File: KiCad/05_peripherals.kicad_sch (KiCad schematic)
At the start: 35 parts, among them IC501 VEML7700-TT, IC502 DS3231MZ+TRL, U502 DS18B20, U503 LM35-LP, U504 DHT11

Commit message: Layout updates
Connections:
- net +3V3 is gone; now on net +3V3_PER: SW501.1, SW501.4, SW502.1, SW502.4, SW503.1, SW503.4
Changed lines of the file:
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@@
 	)
 	(symbol
+		(lib_id "power:+3.3V")
+		(at 55.88 167.64 0)
+		(unit 1)
+		(exclude_from_sim no)
+		(in_bom yes)
+		(on_board yes)
+		(dnp no)
+		(property "Reference" "#PWR02"
+			(at 55.88 171.45 0)
+			(effects
+				(font
+					(size 1.27 1.27)
+				)
+				(hide yes)
+			)
+		)
+		(property "Value" "+3V3_PER"
+			(at 61.214 166.878 0)
+			(effects
+				(font
+					(size 1.27 1.27)
+				)
+			)
+		)
+		(property "Footprint" ""
+			(at 55.88 167.64 0)
+			(effects
+				(font
+					(size 1.27 1.27)
+				)
+				(hide yes)
+			)
+		)
+		(property "Datasheet" ""
+			(at 55.88 167.64 0)
+			(effects
+				(font
+					(size 1.27 1.27)
+				)
+				(hide yes)
+			)
+		)
+		(property "Description" "Power symbol creates a global label with name \"+3.3V\""
+			(at 55.88 167.64 0)
+			(effects
+				(font
+					(size 1.27 1.27)
+				)
+				(hide yes)
+			)
+		)
+		(pin "1"
+		)
+		(instances
+			(project "esp32_s3_weather_webserver"
+				(path "/04e96486-ec4c-4881-a0bf-37cb6ce91c2d/c3c48617-55df-481a-bcdd-56b688125780"
+					(reference "#PWR02")
+					(unit 1)
+				)
+			)
+		)
+	)
+	(symbol
 		(lib_id "power:GND")
 		(at 205.74 116.84 0)
@@
 	)
 	(symbol
-		(lib_id "power:+3.3V")
-		(at 17.78 167.64 0)
-		(unit 1)
-		(exclude_from_sim no)
-		(in_bom yes)
-		(on_board yes)
-		(dnp no)
-		(property "Reference" "#PWR0528"
-			(at 17.78 171.45 0)
-			(effects
-				(font
-					(size 1.27 1.27)
-				)
-				(hide yes)
-			)
-		)
-		(property "Value" "+3V3"
-			(at 17.526 164.338 0)
-			(effects
-				(font
-					(size 1.27 1.27)
-				)
-			)
-		)
-		(property "Footprint" ""
-			(at 17.78 167.64 0)
-			(effects
-				(font
-					(size 1.27 1.27)
-				)
-				(hide yes)
-			)
-		)
-		(property "Datasheet" ""
-			(at 17.78 167.64 0)
-			(effects
-				(font
-					(size 1.27 1.27)
-				)
-				(hide yes)
-			)
-		)
-		(property "Description" "Power symbol creates a global label with name \"+3.3V\""
-			(at 17.78 167.64 0)
-			(effects
-				(font
-					(size 1.27 1.27)
-				)
-				(hide yes)
-			)
-		)
-		(pin "1"
-		)
-		(instances
-			(project "esp32_s3_weather_webserver"
-				(path "/04e96486-ec4c-4881-a0bf-37cb6ce91c2d/c3c48617-55df-481a-bcdd-56b688125780"
-					(reference "#PWR0528")
-					(unit 1)
-				)
-			)
-		)
-	)
-	(symbol
 		(lib_id "esp32_s3_weather_webserver:SW_PUSH_6mm_H5mm")
 		(at 25.4 175.26 0)
@@
 	)
 	(symbol
+		(lib_id "power:+3.3V")
+		(at 99.06 167.64 0)
+		(unit 1)
+		(exclude_from_sim no)
+		(in_bom yes)
+		(on_board yes)
+		(dnp no)
+		(property "Reference" "#PWR01"
+			(at 99.06 171.45 0)
+			(effects
+				(font
+					(size 1.27 1.27)
+				)
+				(hide yes)
+			)
+		)
+		(property "Value" "+3V3_PER"
+			(at 104.394 166.878 0)
+			(effects
+				(font
+					(size 1.27 1.27)
+				)
+			)
+		)
+		(property "Footprint" ""
+			(at 99.06 167.64 0)
+			(effects
+				(font
+					(size 1.27 1.27)
+				)
+				(hide yes)
+			)
+		)
+		(property "Datasheet" ""
+			(at 99.06 167.64 0)
+			(effects
+				(font
+					(size 1.27 1.27)
+				)
+				(hide yes)
+			)
+		)
+		(property "Description" "Power symbol creates a global label with name \"+3.3V\""
+			(at 99.06 167.64 0)
+			(effects
+				(font
+					(size 1.27 1.27)
+				)
+				(hide yes)
+			)
+		)
+		(pin "1"
+		)
+		(instances
+			(project "esp32_s3_weather_webserver"
+				(path "/04e96486-ec4c-4881-a0bf-37cb6ce91c2d/c3c48617-55df-481a-bcdd-56b688125780"
+					(reference "#PWR01")
+					(unit 1)
+				)
+			)
+		)
+	)
+	(symbol
 		(lib_id "esp32_s3_weather_webserver:SW_PUSH_6mm_H5mm")
 		(at 106.68 175.26 0)
@@
 	)
 	(symbol
-		(lib_id "power:+3.3V")
-		(at 55.88 167.64 0)
-		(unit 1)
-		(exclude_from_sim no)
-		(in_bom yes)
-		(on_board yes)
-		(dnp no)
-		(property "Reference" "#PWR0529"
-			(at 55.88 171.45 0)
-			(effects
-				(font
-					(size 1.27 1.27)
-				)
-				(hide yes)
-			)
-		)
-		(property "Value" "+3V3"
-			(at 55.626 164.338 0)
-			(effects
-				(font
-					(size 1.27 1.27)
-				)
-			)
-		)
-		(property "Footprint" ""
-			(at 55.88 167.64 0)
-			(effects
-				(font
-					(size 1.27 1.27)
-				)
-				(hide yes)
-			)
-		)
-		(property "Datasheet" ""
-			(at 55.88 167.64 0)
-			(effects
-				(font
-					(size 1.27 1.27)
-				)
-				(hide yes)
-			)
-		)
-		(property "Description" "Power symbol creates a global label with name \"+3.3V\""
-			(at 55.88 167.64 0)
-			(effects
-				(font
-					(size 1.27 1.27)
-				)
-				(hide yes)
-			)
-		)
-		(pin "1"
-		)
-		(instances
-			(project "esp32_s3_weather_webserver"
-				(path "/04e96486-ec4c-4881-a0bf-37cb6ce91c2d/c3c48617-55df-481a-bcdd-56b688125780"
-					(reference "#PWR0529")
-					(unit 1)
-				)
-			)
-		)
-	)
-	(symbol
 		(lib_id "Device:C")
 		(at 224.79 111.76 0)
@@
 	)
 	(symbol
+		(lib_id "power:+3.3V")
+		(at 17.78 167.64 0)
+		(unit 1)
+		(exclude_from_sim no)
+		(in_bom yes)
+		(on_board yes)
+		(dnp no)
+		(property "Reference" "#PWR03"
+			(at 17.78 171.45 0)
+			(effects
+				(font
+					(size 1.27 1.27)
+				)
+				(hide yes)
+			)
+		)
+		(property "Value" "+3V3_PER"
+			(at 23.368 166.878 0)
+			(effects
+				(font
+					(size 1.27 1.27)
+				)
+			)
+		)
+		(property "Footprint" ""
+			(at 17.78 167.64 0)
+			(effects
+				(font
+					(size 1.27 1.27)
+				)
+				(hide yes)
+			)
+		)
+		(property "Datasheet" ""
+			(at 17.78 167.64 0)
+			(effects
+				(font
+					(size 1.27 1.27)
+				)
+				(hide yes)
+			)
+		)
+		(property "Description" "Power symbol creates a global label with name \"+3.3V\""
+			(at 17.78 167.64 0)
+			(effects
+				(font
+					(size 1.27 1.27)
+				)
+				(hide yes)
+			)
+		)
+		(pin "1"
+		)
+		(instances
+			(project "esp32_s3_weather_webserver"
+				(path "/04e96486-ec4c-4881-a0bf-37cb6ce91c2d/c3c48617-55df-481a-bcdd-56b688125780"
+					(reference "#PWR03")
+					(unit 1)
+				)
+			)
+		)
+	)
+	(symbol
 		(lib_id "Sensor_Temperature:DS18B20")
 		(at 250.19 82.55 0)
@@
 					(unit 1)
 				)
-			)
-		)
-	)
-	(symbol
-		(lib_id "power:+3.3V")
-		(at 99.06 167.64 0)
-		(unit 1)
-		(exclude_from_sim no)
-		(in_bom yes)
-		(on_board yes)
-		(dnp no)
-		(property "Reference" "#PWR0530"
-			(at 99.06 171.45 0)
-			(effects
-				(font
-					(size 1.27 1.27)
-				)
-				(hide yes)
-			)
-		)
-		(property "Value" "+3V3"
-			(at 98.806 164.338 0)
-			(effects
-				(font
-					(size 1.27 1.27)
-				)
-			)
-		)
-		(property "Footprint" ""
-			(at 99.06 167.64 0)
-			(effects
-				(font
-					(size 1.27 1.27)
-				)
-				(hide yes)
-			)
-		)
-		(property "Datasheet" ""
-			(at 99.06 167.64 0)
-			(effects
-				(font
-					(size 1.27 1.27)
-				)
-				(hide yes)
-			)
-		)
-		(property "Description" "Power symbol creates a global label with name \"+3.3V\""
-			(at 99.06 167.64 0)
-			(effects
-				(font
-					(size 1.27 1.27)
-				)
-				(hide yes)
-			)
-		)
-		(pin "1"
-		)
-		(instances
-			(project "esp32_s3_weather_webserver"
-				(path "/04e96486-ec4c-4881-a0bf-37cb6ce91c2d/c3c48617-55df-481a-bcdd-56b688125780"
-					(reference "#PWR0530")
-					(unit 1)
-				)

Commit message: SPI signals routing
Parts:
- BT501: footprint esp32_s3_weather_webserver:CR12202 -> esp32_s3_weather_webserver:MPD_BC2032-E2; Manufacturer Q&J -> MYOUNG; Manufacturer Part Number CR1220-2 -> BS-02-A1AJ010
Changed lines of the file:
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@@
 			)
 		)
-		(property "Footprint" "esp32_s3_weather_webserver:CR12202"
+		(property "Footprint" "esp32_s3_weather_webserver:MPD_BC2032-E2"
 			(at 84.836 119.38 90)
 			(effects
@@
 			)
 		)
-		(property "Manufacturer" "Q&J"
+		(property "Manufacturer" "MYOUNG"
 			(at 86.36 119.38 0)
 			(effects
@@
 			)
 		)
-		(property "Manufacturer Part Number" "CR1220-2"
+		(property "Manufacturer Part Number" "BS-02-A1AJ010"
 			(at 86.36 119.38 0)
 			(effects

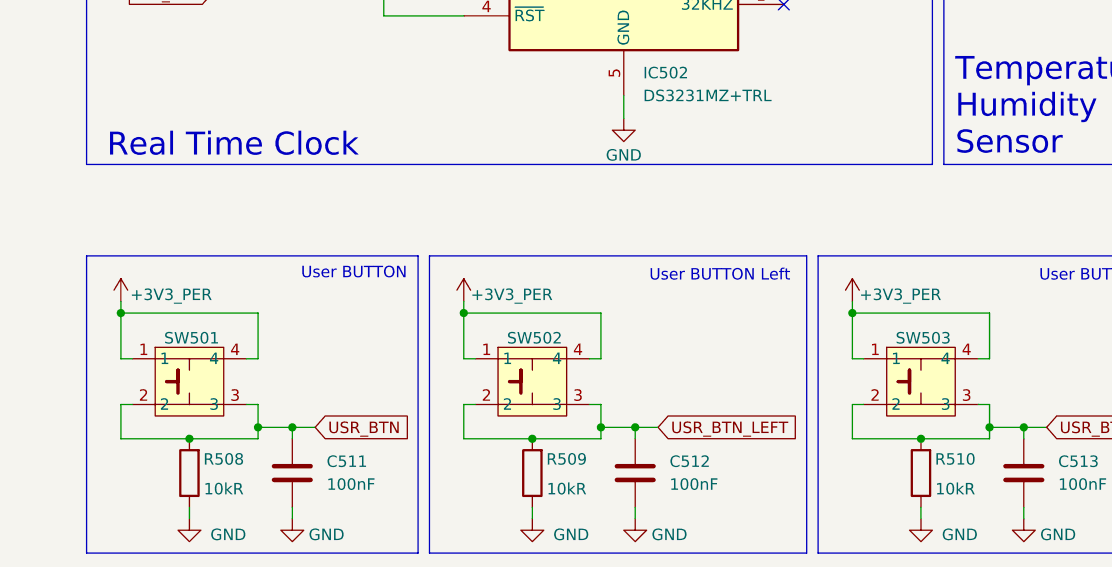
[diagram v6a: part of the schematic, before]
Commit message: Signal routing
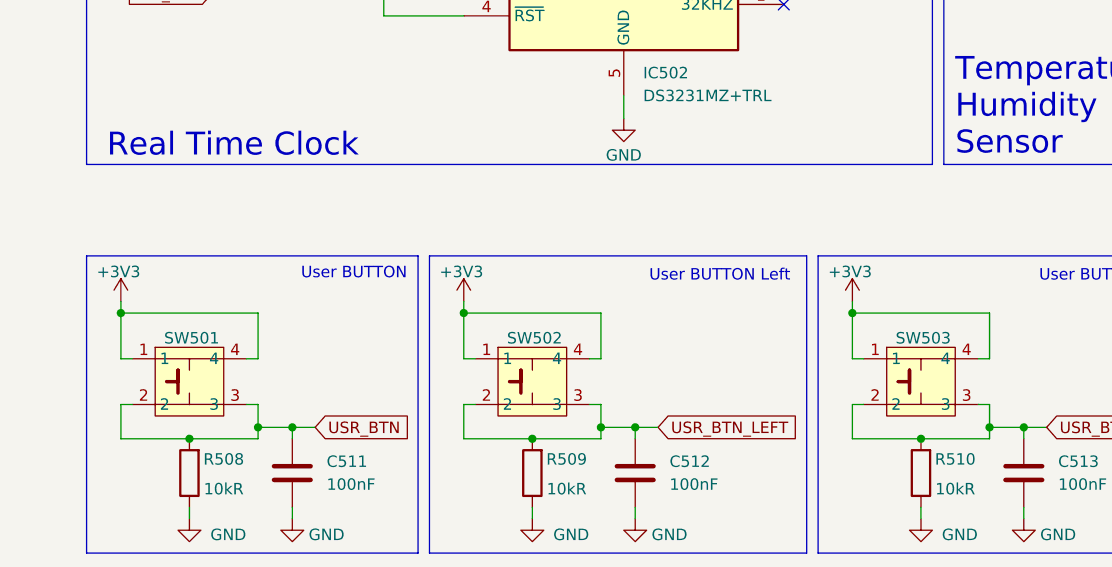
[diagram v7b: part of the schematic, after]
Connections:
- net +3V3_PER: no longer SW501.1, SW501.4, SW502.1, SW502.4, SW503.1, SW503.4
- new net +3V3: SW501.1, SW501.4, SW502.1, SW502.4, SW503.1, SW503.4

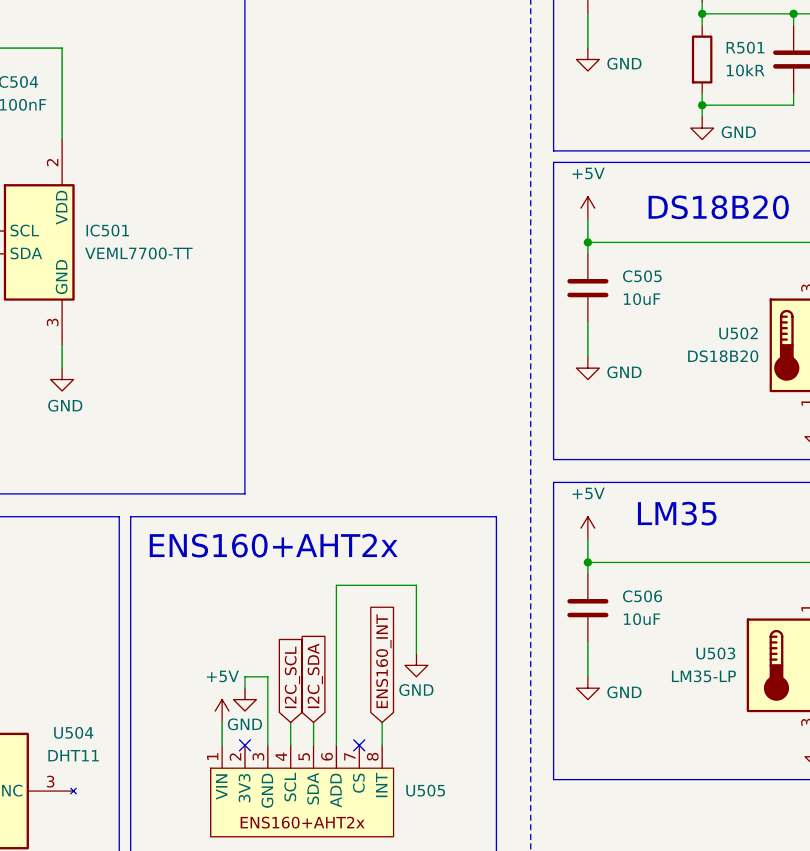
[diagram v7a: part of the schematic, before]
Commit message: Add battery connector and charger
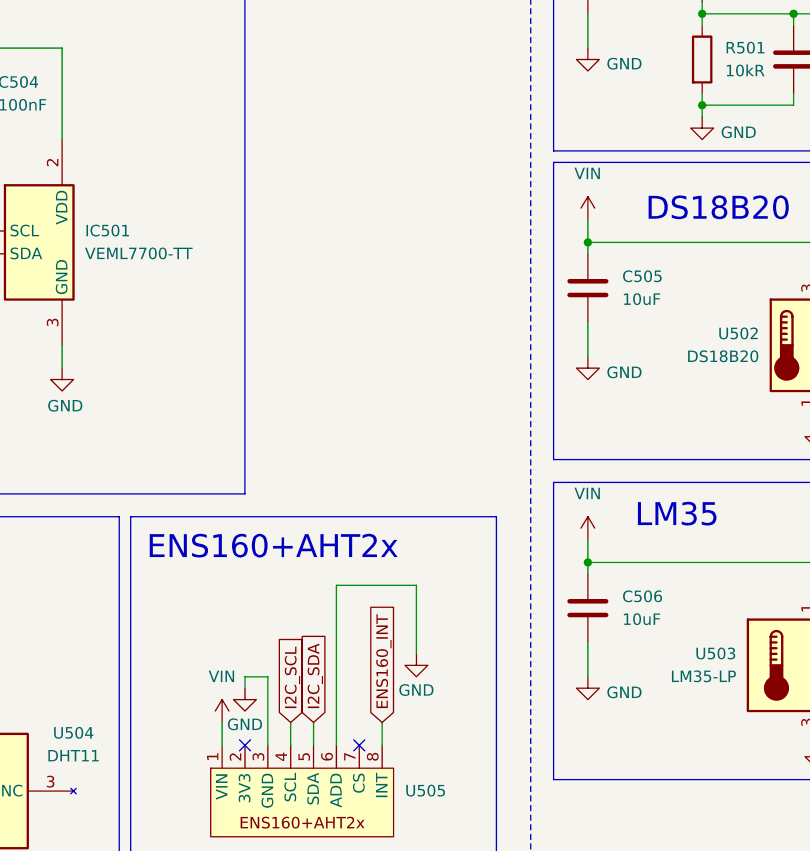
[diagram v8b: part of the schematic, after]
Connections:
- net +5V renamed VIN
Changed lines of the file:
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@@
+	)
+	(symbol
+		(lib_id "power:+5V")
+		(at 184.15 124.46 0)
+		(mirror y)
+		(unit 1)
+		(exclude_from_sim no)
+		(in_bom yes)
+		(on_board yes)
+		(dnp no)
+		(fields_autoplaced yes)
+		(property "Reference" "#PWR0523"
+			(at 184.15 128.27 0)
+			(effects
+				(font
+					(size 1.27 1.27)
+				)
+				(hide yes)
+			)
+		)
+		(property "Value" "VIN"
+			(at 184.15 119.38 0)
+			(effects
+				(font
+					(size 1.27 1.27)
+				)
+			)
+		)
+		(property "Footprint" ""
+			(at 184.15 124.46 0)
+			(effects
+				(font
+					(size 1.27 1.27)
+				)
+				(hide yes)
+			)
+		)
+		(property "Datasheet" ""
+			(at 184.15 124.46 0)
+			(effects
+				(font
+					(size 1.27 1.27)
+				)
+				(hide yes)
+			)
+		)
+		(property "Description" "Power symbol creates a global label with name \"+5V\""
+			(at 184.15 124.46 0)
+			(effects
+				(font
+					(size 1.27 1.27)
+				)
+				(hide yes)
+			)
+		)
+		(pin "1"
+		)
+		(instances
+			(project "esp32_s3_weather_webserver"
+				(path "/04e96486-ec4c-4881-a0bf-37cb6ce91c2d/c3c48617-55df-481a-bcdd-56b688125780"
+					(reference "#PWR0523")
+					(unit 1)
+				)
+			)
+		)
 	)
 	(symbol
@@
 	)
 	(symbol
+		(lib_id "power:+5V")
+		(at 224.79 68.58 0)
+		(mirror y)
+		(unit 1)
+		(exclude_from_sim no)
+		(in_bom yes)
+		(on_board yes)
+		(dnp no)
+		(fields_autoplaced yes)
+		(property "Reference" "#PWR0508"
+			(at 224.79 72.39 0)
+			(effects
+				(font
+					(size 1.27 1.27)
+				)
+				(hide yes)
+			)
+		)
+		(property "Value" "VIN"
+			(at 224.79 63.5 0)
+			(effects
+				(font
+					(size 1.27 1.27)
+				)
+			)
+		)
+		(property "Footprint" ""
+			(at 224.79 68.58 0)
+			(effects
+				(font
+					(size 1.27 1.27)
+				)
+				(hide yes)
+			)
+		)
+		(property "Datasheet" ""
+			(at 224.79 68.58 0)
+			(effects
+				(font
+					(size 1.27 1.27)
+				)
+				(hide yes)
+			)
+		)
+		(property "Description" "Power symbol creates a global label with name \"+5V\""
+			(at 224.79 68.58 0)
+			(effects
+				(font
+					(size 1.27 1.27)
+				)
+				(hide yes)
+			)
+		)
+		(pin "1"
+		)
+		(instances
+			(project "esp32_s3_weather_webserver"
+				(path "/04e96486-ec4c-4881-a0bf-37cb6ce91c2d/c3c48617-55df-481a-bcdd-56b688125780"
+					(reference "#PWR0508")
+					(unit 1)
+				)
+			)
+		)
+	)
+	(symbol
 		(lib_id "power:GND")
 		(at 144.78 60.96 0)
@@
 		(on_board yes)
 		(dnp no)
-		(property "Reference" "#PWR03"
+		(property "Reference" "#PWR0528"
 			(at 17.78 171.45 0)
 			(effects
@@
 			(project "esp32_s3_weather_webserver"
 				(path "/04e96486-ec4c-4881-a0bf-37cb6ce91c2d/c3c48617-55df-481a-bcdd-56b688125780"
-					(reference "#PWR03")
+					(reference "#PWR0528")
 					(unit 1)
 				)
@@
 	)
 	(symbol
+		(lib_id "power:+5V")
+		(at 224.79 104.14 0)
+		(mirror y)
+		(unit 1)
+		(exclude_from_sim no)
+		(in_bom yes)
+		(on_board yes)
+		(dnp no)
+		(fields_autoplaced yes)
+		(property "Reference" "#PWR0513"
+			(at 224.79 107.95 0)
+			(effects
+				(font
+					(size 1.27 1.27)
+				)
+				(hide yes)
+			)
+		)
+		(property "Value" "VIN"
+			(at 224.79 99.06 0)
+			(effects
+				(font
+					(size 1.27 1.27)
+				)
+			)
+		)
+		(property "Footprint" ""
+			(at 224.79 104.14 0)
+			(effects
+				(font
+					(size 1.27 1.27)
+				)
+				(hide yes)
+			)
+		)
+		(property "Datasheet" ""
+			(at 224.79 104.14 0)
+			(effects
+				(font
+					(size 1.27 1.27)
+				)
+				(hide yes)
+			)
+		)
+		(property "Description" "Power symbol creates a global label with name \"+5V\""
+			(at 224.79 104.14 0)
+			(effects
+				(font
+					(size 1.27 1.27)
+				)
+				(hide yes)
+			)
+		)
+		(pin "1"
+		)
+		(instances
+			(project "esp32_s3_weather_webserver"
+				(path "/04e96486-ec4c-4881-a0bf-37cb6ce91c2d/c3c48617-55df-481a-bcdd-56b688125780"
+					(reference "#PWR0513")
+					(unit 1)
+				)
+			)
+		)
+	)
+	(symbol
 		(lib_id "Device:C")
 		(at 224.79 111.76 0)
@@
 	)
 	(symbol
-		(lib_id "power:+5V")
-		(at 224.79 104.14 0)
-		(mirror y)
-		(unit 1)
-		(exclude_from_sim no)
-		(in_bom yes)
-		(on_board yes)
-		(dnp no)
-		(fields_autoplaced yes)
-		(property "Reference" "#PWR0513"
-			(at 224.79 107.95 0)
-			(effects
-				(font
-					(size 1.27 1.27)
-				)
-				(hide yes)
-			)
-		)
-		(property "Value" "+5V"
-			(at 224.79 99.06 0)
-			(effects
-				(font
-					(size 1.27 1.27)
-				)
-			)
-		)
-		(property "Footprint" ""
-			(at 224.79 104.14 0)
-			(effects
-				(font
-					(size 1.27 1.27)
-				)
-				(hide yes)
-			)
-		)
-		(property "Datasheet" ""
-			(at 224.79 104.14 0)
-			(effects
-				(font
-					(size 1.27 1.27)
-				)
-				(hide yes)
-			)
-		)
-		(property "Description" "Power symbol creates a global label with name \"+5V\""
-			(at 224.79 104.14 0)
-			(effects
-				(font
-					(size 1.27 1.27)
-				)
-				(hide yes)
-			)
-		)
-		(pin "1"
-		)
-		(instances
-			(project "esp32_s3_weather_webserver"
-				(path "/04e96486-ec4c-4881-a0bf-37cb6ce91c2d/c3c48617-55df-481a-bcdd-56b688125780"
-					(reference "#PWR0513")
-					(unit 1)
-				)
-			)
-		)
-	)
-	(symbol
 		(lib_id "Device:C")
 		(at 134.62 119.38 0)
@@
 		(on_board yes)
 		(dnp no)
-		(property "Reference" "#PWR02"
+		(property "Reference" "#PWR0529"
 			(at 55.88 171.45 0)
 			(effects
@@
 			(project "esp32_s3_weather_webserver"
 				(path "/04e96486-ec4c-4881-a0bf-37cb6ce91c2d/c3c48617-55df-481a-bcdd-56b688125780"
-					(reference "#PWR02")
+					(reference "#PWR0529")
 					(unit 1)
 				)
@@
 	)
 	(symbol
-		(lib_id "power:+5V")
-		(at 224.79 68.58 0)
-		(mirror y)
-		(unit 1)
-		(exclude_from_sim no)
-		(in_bom yes)
-		(on_board yes)
-		(dnp no)
-		(fields_autoplaced yes)
-		(property "Reference" "#PWR0508"
-			(at 224.79 72.39 0)
-			(effects
-				(font
-					(size 1.27 1.27)
-				)
-				(hide yes)
-			)
-		)
-		(property "Value" "+5V"
-			(at 224.79 63.5 0)
-			(effects
-				(font
-					(size 1.27 1.27)
-				)
-			)
-		)
-		(property "Footprint" ""
-			(at 224.79 68.58 0)
-			(effects
-				(font
-					(size 1.27 1.27)
-				)
-				(hide yes)
-			)
-		)
-		(property "Datasheet" ""
-			(at 224.79 68.58 0)
-			(effects
-				(font
-					(size 1.27 1.27)
-				)
-				(hide yes)
-			)
-		)
-		(property "Description" "Power symbol creates a global label with name \"+5V\""
-			(at 224.79 68.58 0)
-			(effects
-				(font
-					(size 1.27 1.27)
-				)
-				(hide yes)
-			)
-		)
-		(pin "1"
-		)
-		(instances
-			(project "esp32_s3_weather_webserver"
-				(path "/04e96486-ec4c-4881-a0bf-37cb6ce91c2d/c3c48617-55df-481a-bcdd-56b688125780"
-					(reference "#PWR0508")
-					(unit 1)
-				)
-			)
-		)
-	)
-	(symbol
 		(lib_id "power:+3.3V")
 		(at 123.19 113.03 0)
@@
 	)
 	(symbol
-		(lib_id "power:+5V")
-		(at 184.15 124.46 0)
-		(mirror y)
-		(unit 1)
-		(exclude_from_sim no)
-		(in_bom yes)
-		(on_board yes)
-		(dnp no)
-		(fields_autoplaced yes)
-		(property "Reference" "#PWR0523"
-			(at 184.15 128.27 0)
-			(effects
-				(font
-					(size 1.27 1.27)
-				)
-				(hide yes)
-			)
-		)
-		(property "Value" "+5V"
-			(at 184.15 119.38 0)
-			(effects
-				(font
-					(size 1.27 1.27)
-				)
-			)
-		)
-		(property "Footprint" ""
-			(at 184.15 124.46 0)
-			(effects
-				(font
-					(size 1.27 1.27)
-				)
-				(hide yes)
-			)
-		)
-		(property "Datasheet" ""
-			(at 184.15 124.46 0)
-			(effects
-				(font
-					(size 1.27 1.27)
-				)
-				(hide yes)
-			)
-		)
-		(property "Description" "Power symbol creates a global label with name \"+5V\""
-			(at 184.15 124.46 0)
-			(effects
-				(font
-					(size 1.27 1.27)
-				)
-				(hide yes)
-			)
-		)
-		(pin "1"
-		)
-		(instances
-			(project "esp32_s3_weather_webserver"
-				(path "/04e96486-ec4c-4881-a0bf-37cb6ce91c2d/c3c48617-55df-481a-bcdd-56b688125780"
-					(reference "#PWR0523")
-					(unit 1)
-				)
-			)
-		)
-	)
-	(symbol
 		(lib_id "Device:C")
 		(at 74.93 186.69 0)
@@
 		(on_board yes)
 		(dnp no)
-		(property "Reference" "#PWR01"
+		(property "Reference" "#PWR0530"
 			(at 99.06 171.45 0)
 			(effects
@@
 			(project "esp32_s3_weather_webserver"
 				(path "/04e96486-ec4c-4881-a0bf-37cb6ce91c2d/c3c48617-55df-481a-bcdd-56b688125780"
-					(reference "#PWR01")
-					(unit 1)
-				)
+					(reference "#PWR0530")
+					(unit 1)
+				)
